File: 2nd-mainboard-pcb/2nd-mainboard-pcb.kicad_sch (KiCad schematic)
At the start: 3 parts, among them J1 USB_C_Receptacle, U1 ATmega328PB-A, U2 FT232RL

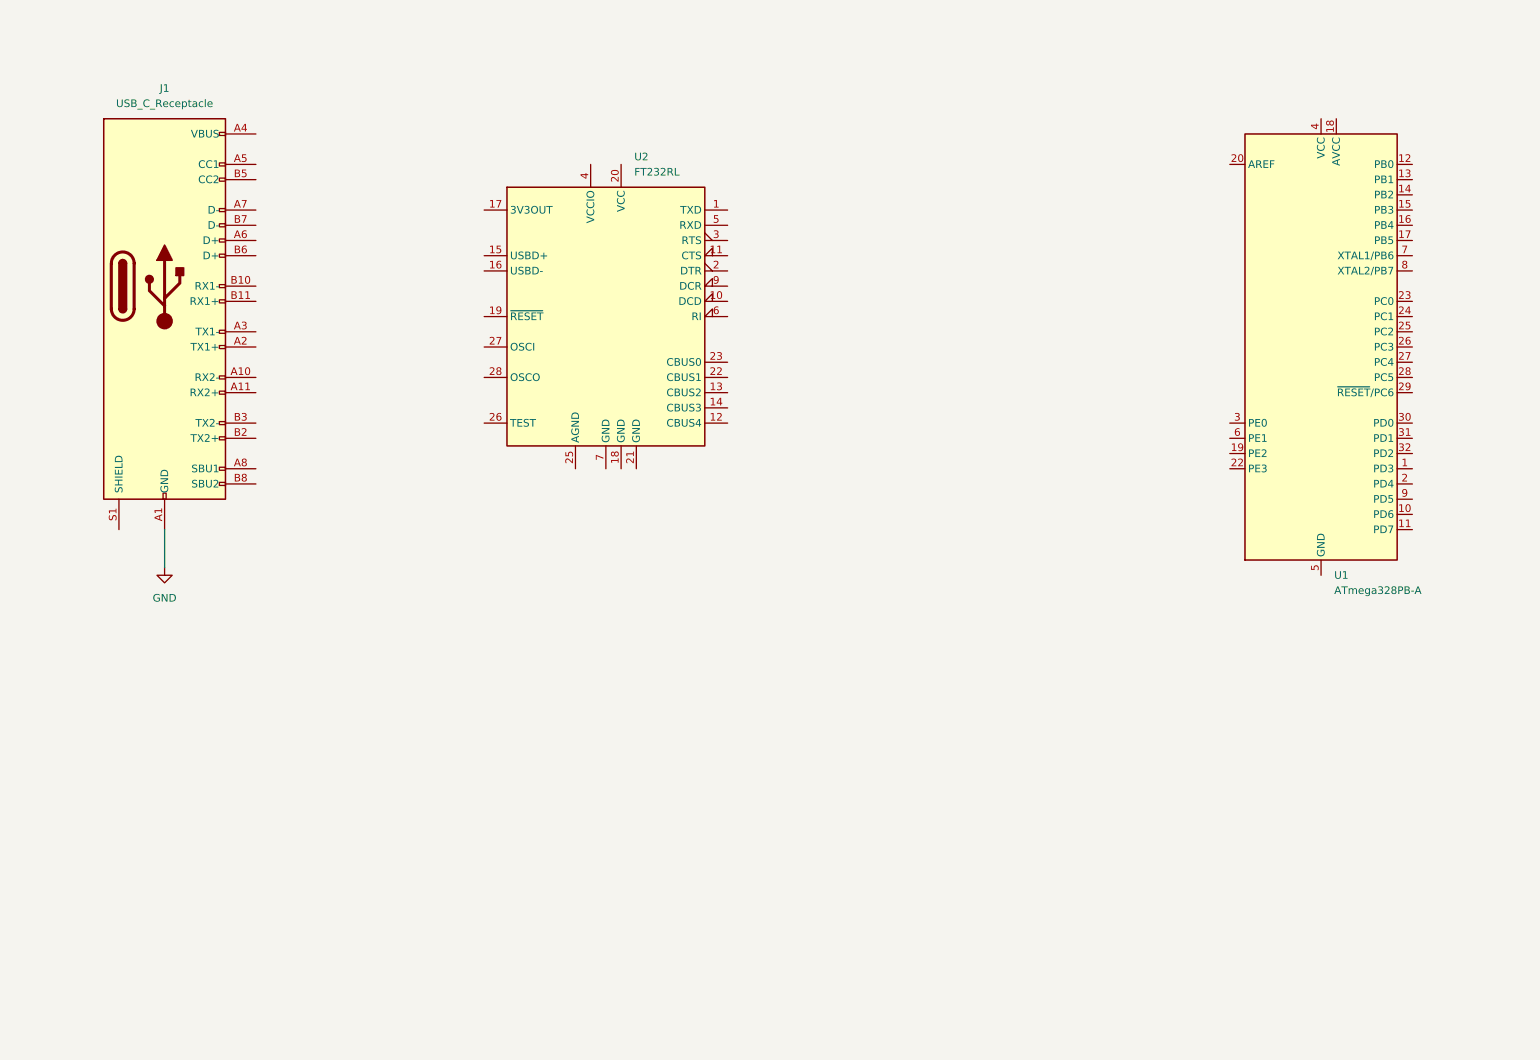
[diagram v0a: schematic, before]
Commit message: added basic logic
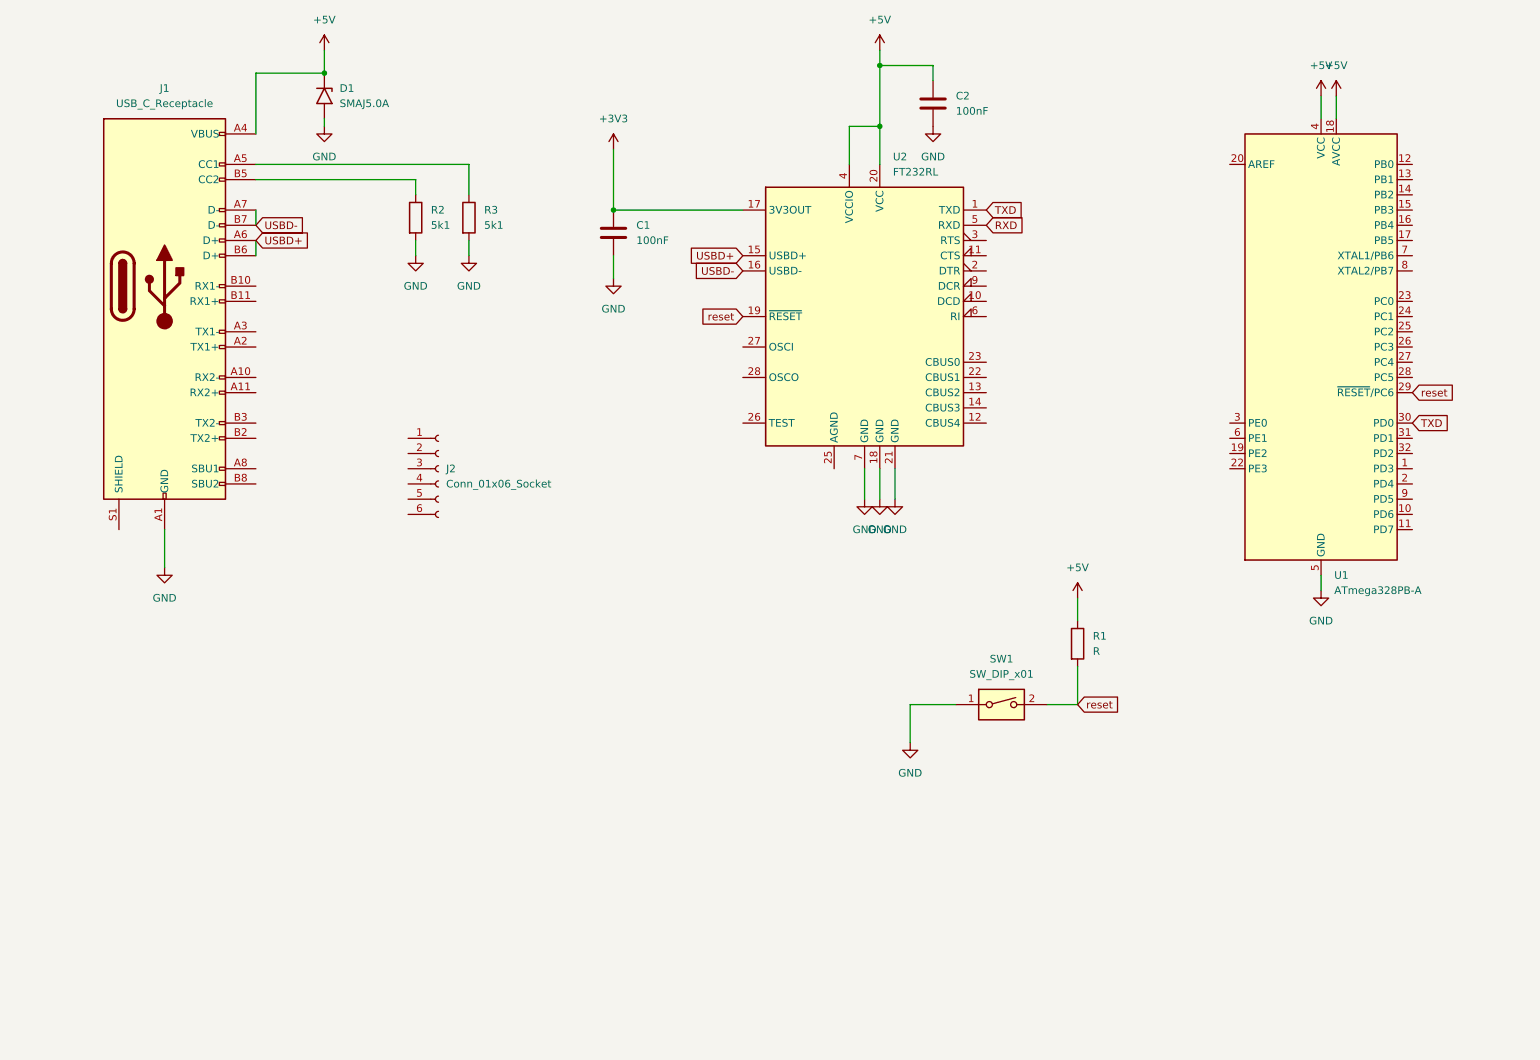
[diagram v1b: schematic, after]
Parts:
- added C1, C2: 100nF, symbol Device:C
- added D1: SMAJ5.0A, Diode_SMD:D_SMA, symbol Diode:SMAJ5.0A
- added J2: Conn_01x06_Socket, symbol Connector:Conn_01x06_Socket
- added R1: R, symbol Device:R
- added R2, R3: 5k1, symbol Device:R
- added SW1: SW_DIP_x01, Button_Switch_SMD:SW_SPST_EVQQ2, symbol Switch:SW_DIP_x01
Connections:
- net GND: now also U1.21 (GND), U1.5 (GND), U2.18 (GND), U2.21 (GND), U2.7 (GND), C1.2, C2.2, D1.2 (A2), R2.2, R3.2, SW1.1
- net +5V: now reaches J1.A4 (VBUS), J1.A9 (VBUS), J1.B4 (VBUS), J1.B9 (VBUS)
- net +5V: now also U1.18 (AVCC), U1.4 (VCC), U2.20 (VCC), U2.4 (VCCIO), C2.1, D1.1 (A1), R1.1
- net at J1.A5 (CC1): now also R3.1
- net USBD+: now reaches J1.A6 (D+)
- net USBD+: now also J1.B6 (D+), U2.15 (USBD+)
- net USBD-: now reaches J1.A7 (D-)
- net USBD-: now also J1.B7 (D-), U2.16 (USBD-)
- net at J1.B5 (CC2): now also R2.1
- net TXD: now reaches U2.1 (TXD)
- net TXD: now also U1.30 (PD0)
- net +3V3: now reaches U2.17 (3V3OUT)
- net +3V3: now also C1.1
- net reset: now reaches U2.19 (~{RESET})
- net reset: now also U1.29 (~{RESET}/PC6), R1.2, SW1.2
- net RXD: now reaches U2.5 (RXD)
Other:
- moved on the sheet: U2

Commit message: managed libraries
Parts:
- added R4, R5: 10k, symbol Device:R
- R1: value R -> 10k
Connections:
- net +5V: now also R4.1, R5.1
- net RXD: now also U1.31 (PD1)
- net at U2.22 (CBUS1): now also R5.2
- net at U2.23 (CBUS0): now also R4.2
- no-connect marks 0 -> 20

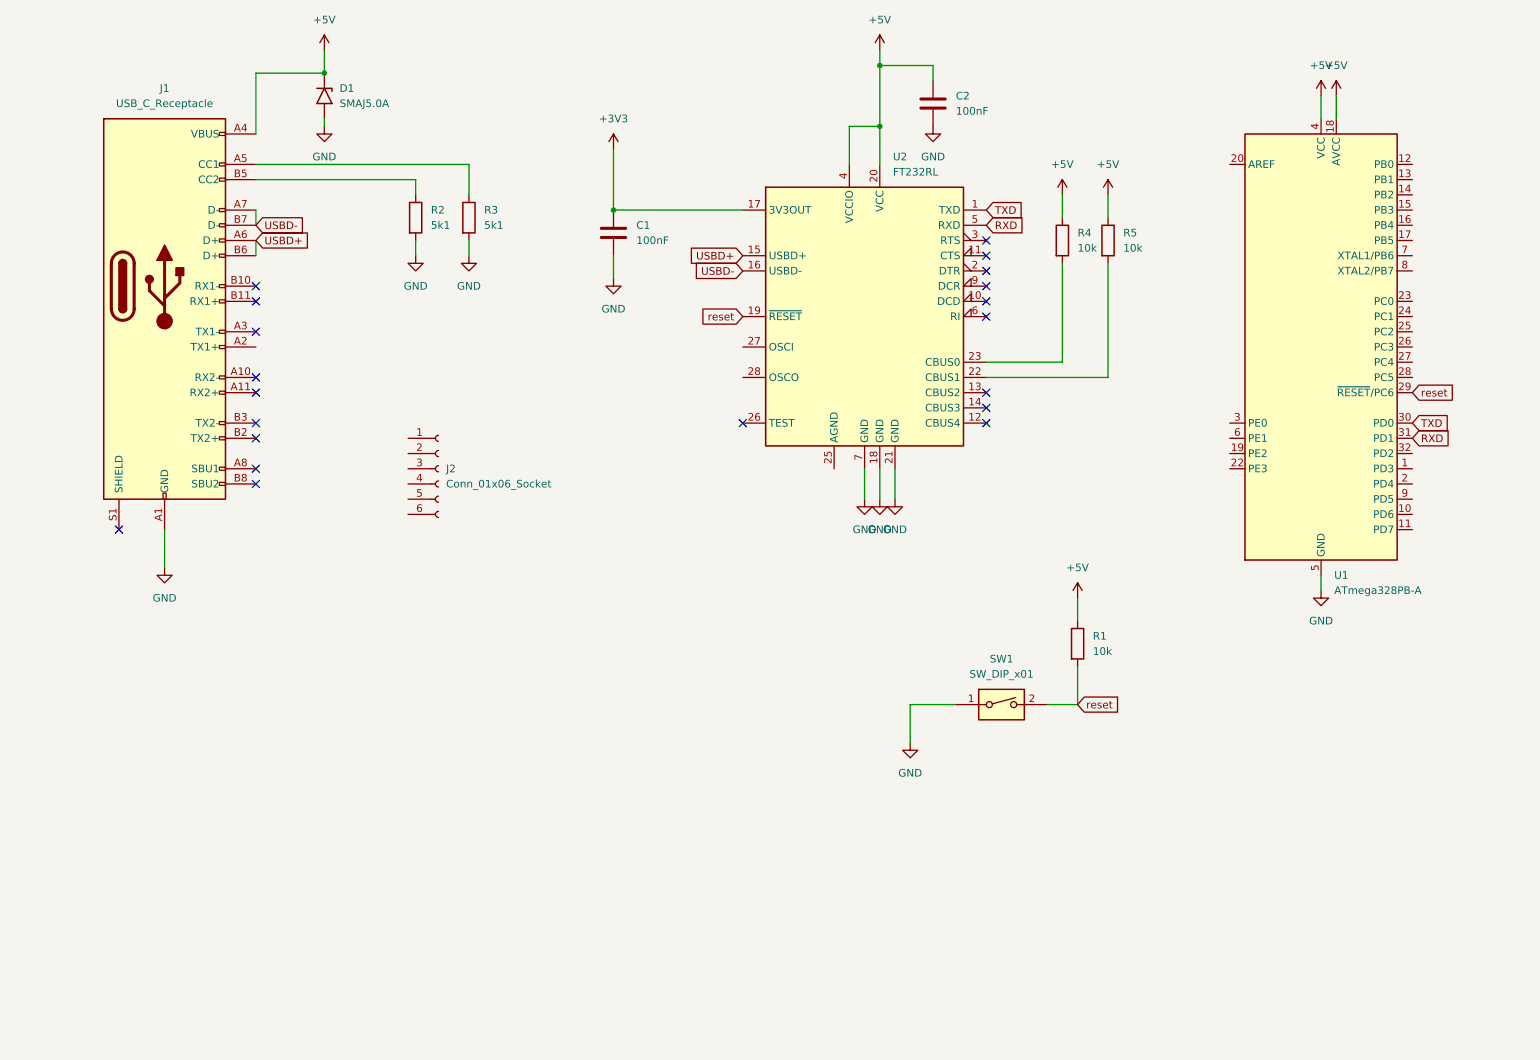
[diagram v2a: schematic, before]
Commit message: added basic peripherie for the atmega and met with group
incoming tasks: pads for unused ios for debugging use cases, add stepper driver, tsv diodes and condensators
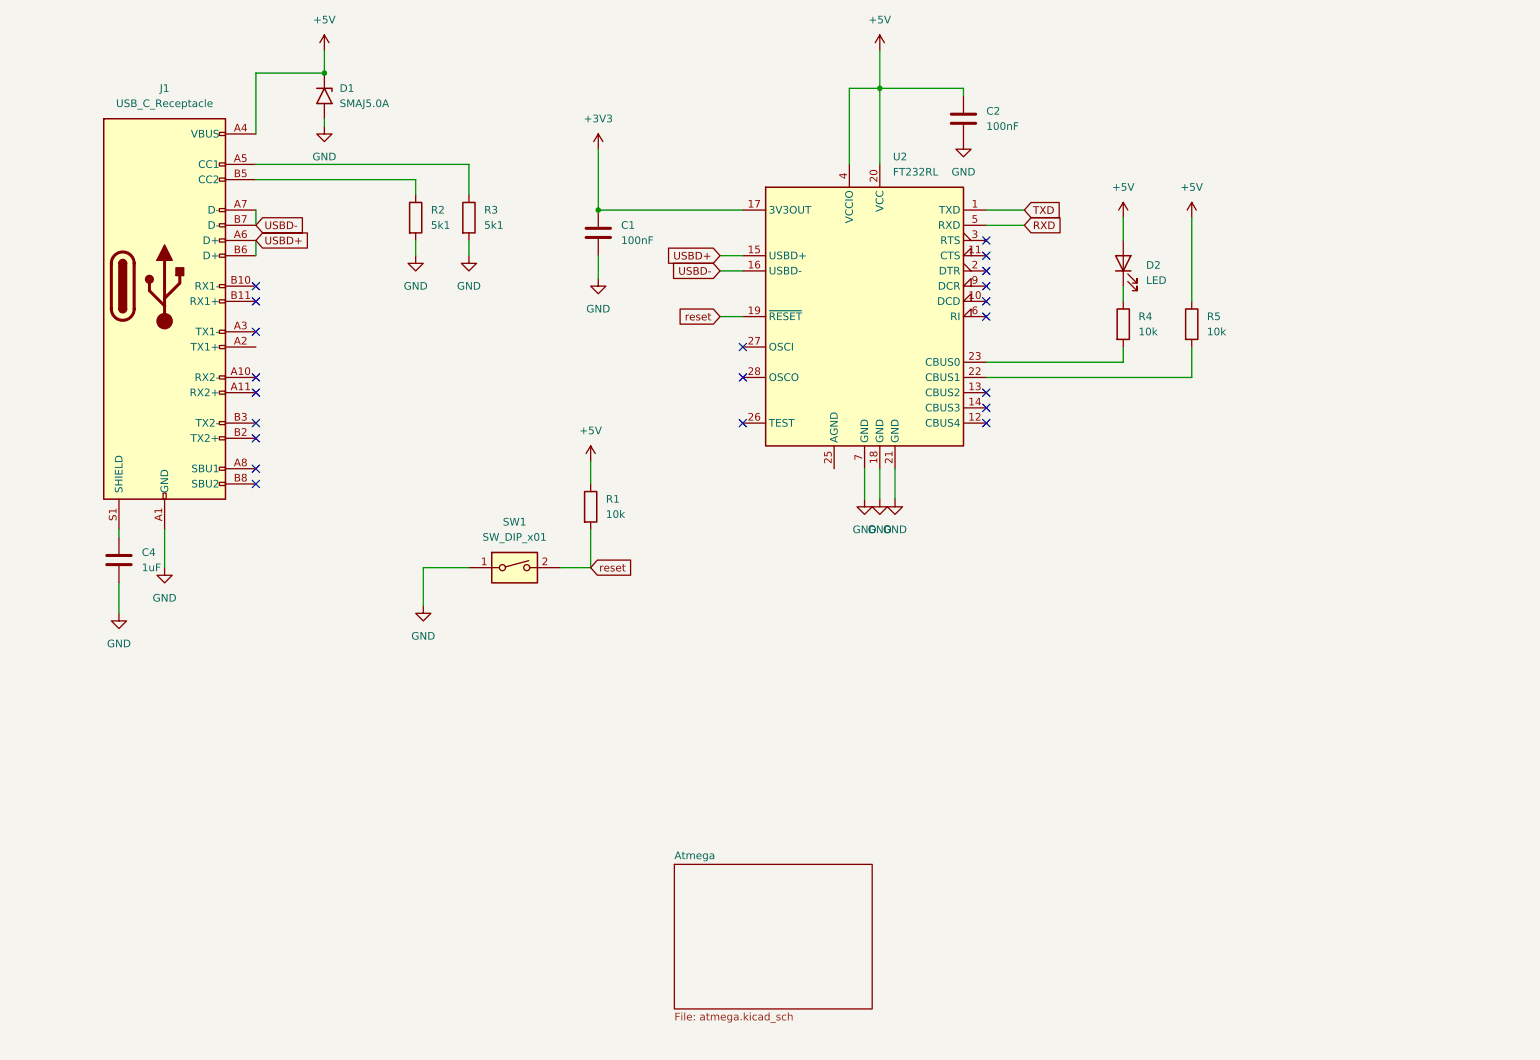
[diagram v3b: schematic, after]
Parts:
- removed J2: Conn_01x06_Socket, symbol Connector:Conn_01x06_Socket
- removed U1: ATmega328PB-A, Package_QFP:TQFP-32_7x7mm_P0.8mm, symbol MCU_Microchip_ATmega:ATmega328PB-A
- added C4: 1uF, symbol Device:C
- added D2: LED, symbol Device:LED
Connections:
- net +5V: now also D2.2 (A); no longer R4.1
- net GND: now also C4.2
- net at J1.S1 (SHIELD): now also C4.1
- new net: D2.1 (K), R4.1
- no-connect marks 20 -> 21
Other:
- added sheet Atmega (atmega.kicad_sch)
- moved on the sheet: C1, C2, R1, R4, R5, SW1

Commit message: added test point and documentation
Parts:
- J1: footprint (none) -> Connector_USB:USB_C_Receptacle_GCT_USB4085
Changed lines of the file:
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@@
 			)
 		)
-		(property "Footprint" ""
+		(property "Footprint" "Connector_USB:USB_C_Receptacle_GCT_USB4085"
 			(at 53.34 66.04 0)
 			(effects

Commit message: jtag funktionalität
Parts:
- added C13: 0.1µF, Capacitor_SMD:CP_Elec_5x3, symbol Device:C_Polarized
- added C15: 0.22µF, Capacitor_SMD:C_0402_1005Metric, symbol Device:C
- added C17: 0.1µF, Capacitor_SMD:C_0402_1005Metric, symbol Device:C
- added J16: Power, symbol Connector:Conn_01x02_Pin
- added JP2: MEASO, Jumper:SolderJumper-2_P1.3mm_Bridged_Pad1.0x1.5mm, symbol Jumper:SolderJumper_2_Bridged
- added R18: 10, symbol Device:R
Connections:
- net GND: now also C13.2, C15.2, C17.2, R18.2
- net reset renamed RESET
- new net: J16.1 (Pin_1), JP2.1 (A)
- new net +12V: C13.1, C15.1, C17.1, JP2.2 (B)
- new net GND2: J16.2 (Pin_2), R18.1
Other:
- added sheet Breakoff Board (breakoff_board.kicad_sch)
- added sheet Motor Driver (motor_driver.kicad_sch)
- note added: "Begrenzgung der Masseströme"
- note added: "Leistungs-Eingang 12V/5V"

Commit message: added libraries
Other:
- added sheet Stacked PCB Design (stacked_pcb.kicad_sch)
- note added: "Da der 3D Drucker nicht immer verlässlich 24V Versorgungsspannung gibt, kann hier ein LM2596 verbaut werden um mögliche 24V auf 12V herunterzuregeln, um die Fans nicht zu schädigne"
- moved on the sheet: C13, C15, C17, J16, JP2, R18
